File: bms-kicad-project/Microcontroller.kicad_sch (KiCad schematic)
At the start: 40 parts, among them J1 12402012E212A, J2 DEBUG, J3 Conn_02x18_Odd_Even, J4 Conn_02x18_Odd_Even, Q1 BSS308PE_H6327, SW1 KMR223G LFG, SW2 KMR223G LFG, U2 W25Q128JVSIQ TR, U3 NCP1117ST33T3G, U4 RP2040, X1 ABM8-272-T3

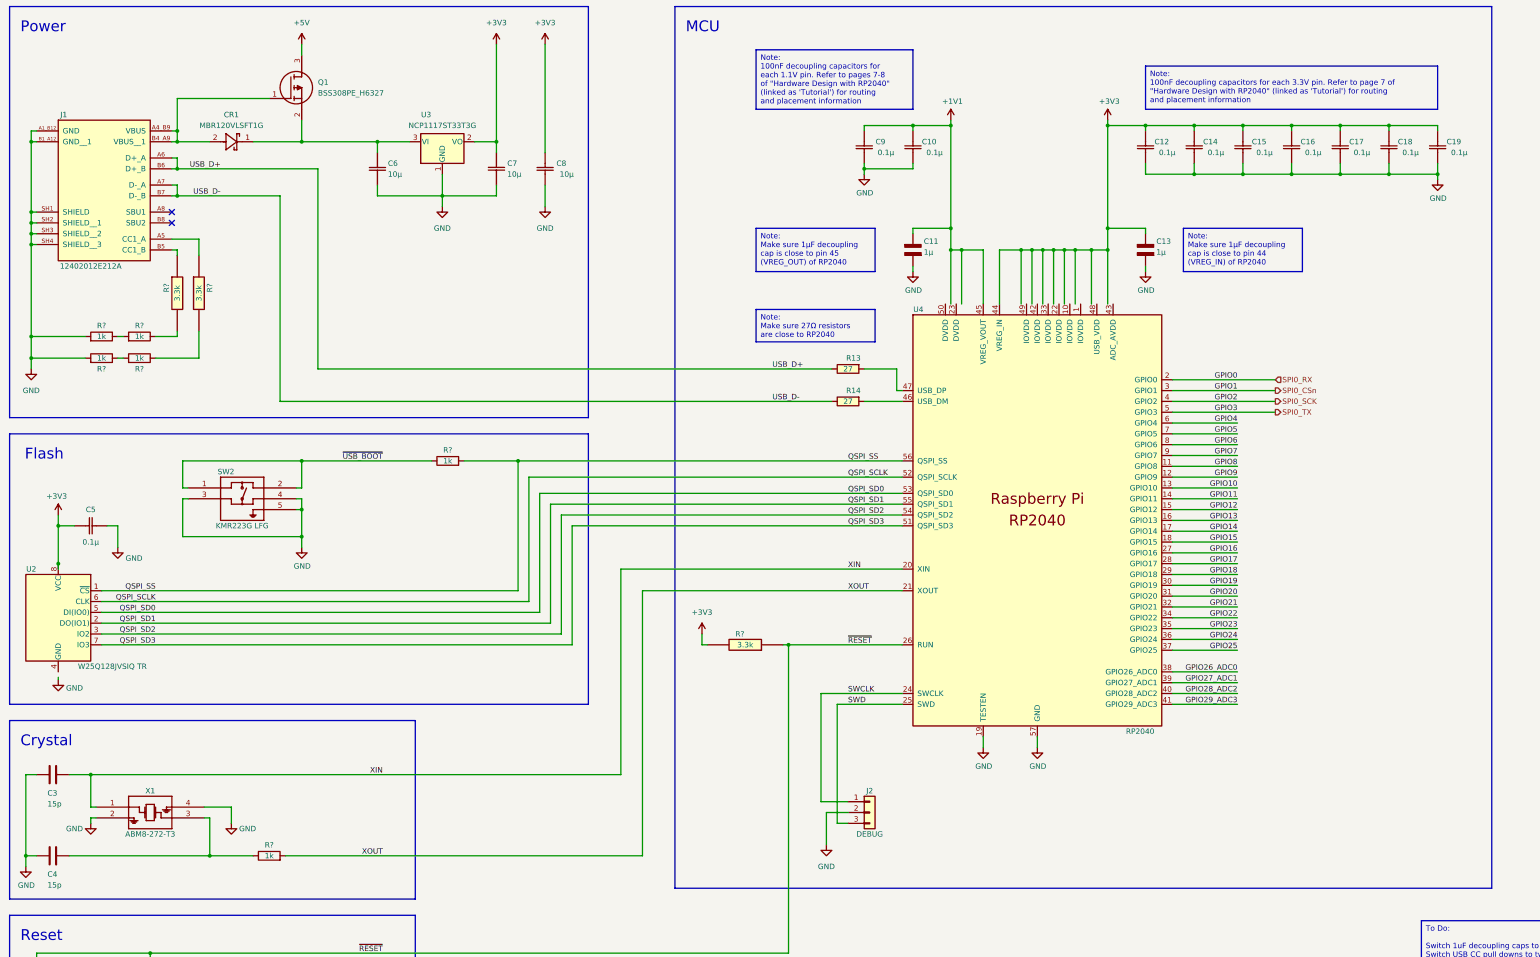
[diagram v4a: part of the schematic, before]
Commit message: feat: Added snubber circuit to 5V Regulator schematic
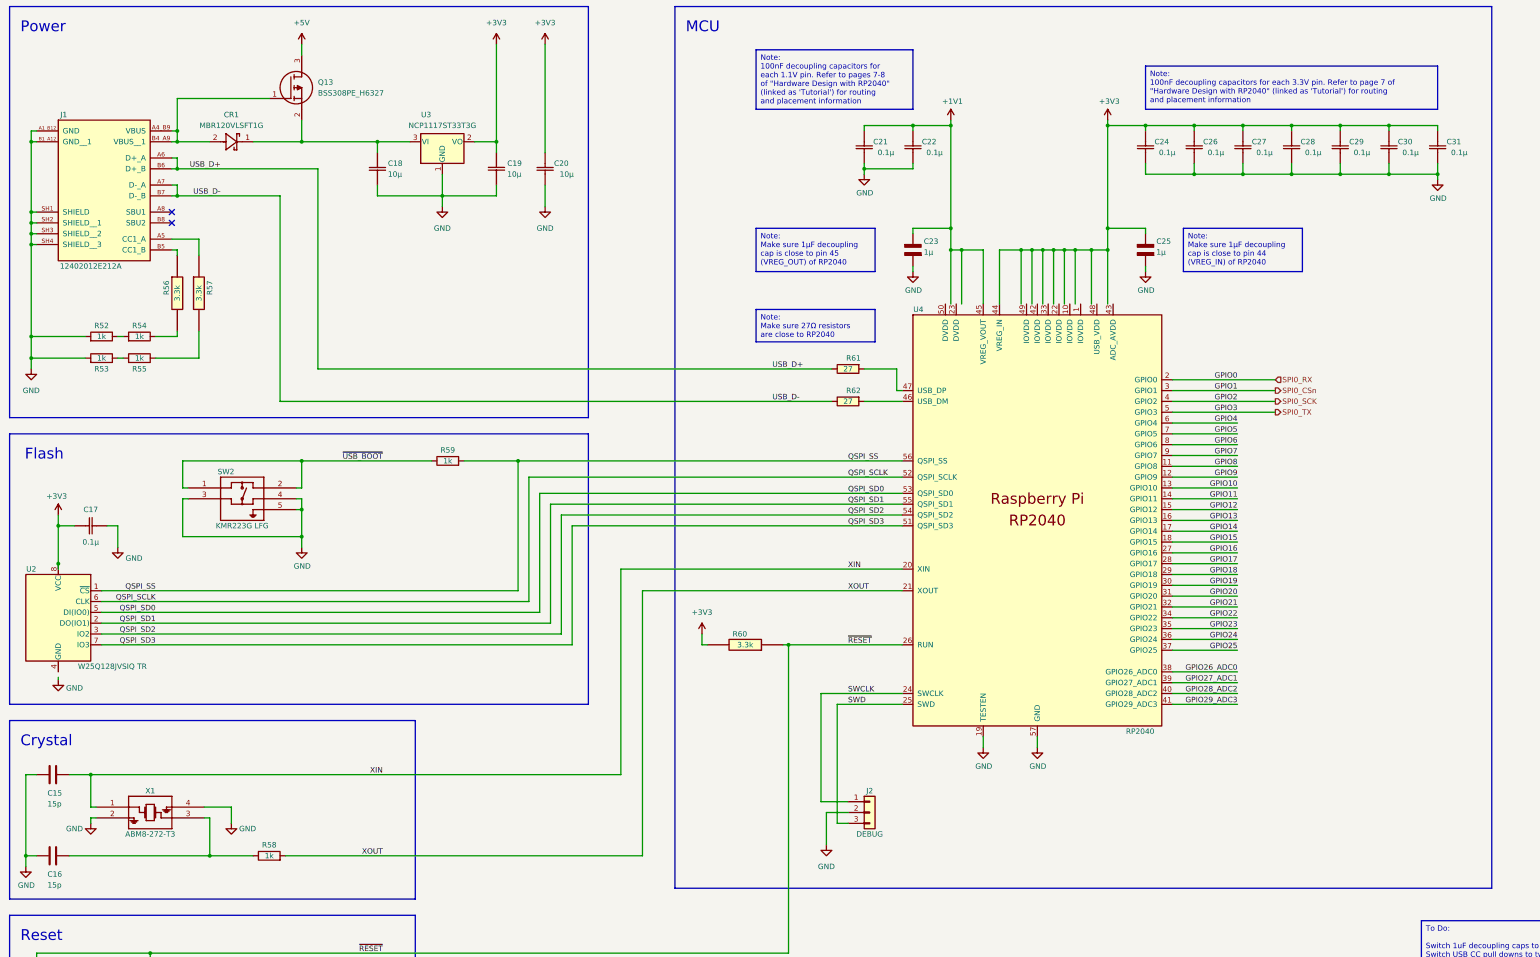
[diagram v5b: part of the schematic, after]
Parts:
- gave numbers to parts that had none: 9
- renumbered C3 to C15, C4 to C16, C5 to C17, C6 to C18, C7 to C19, C8 to C20, C9 to C21, C10 to C22, C11 to C23, C12 to C24, C13 to C25, C14 to C26, C15 to C27, C16 to C28, C17 to C29, C18 to C30, C19 to C31, Q1 to Q13, R13 to R61, R14 to R62

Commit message: feat: added buncha shit, refer to tasks 4 and 8
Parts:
- removed R52, R53, R54, R55: 1k, FixedWing:RC0805N_YAG, symbol FixedWing:RC0805FR-071KL
- removed R56, R57, R60: 3.3k, RESC2012X50N, symbol FixedWing:CRCW08053K30JNEA
- added R77, R78, R81: 5.6k, FixedWing:RESC2012X60N, symbol FixedWing:RK73H2ATTD5601F
- renumbered R58 to R79, R59 to R80, R61 to R82, R62 to R83
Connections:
- net +3V3: now also R81.1
- net GND: now also R77.1, R78.1
- net ~{RESET}: now also R81.2
- net at J1.A5 (CC1_A): now also R78.2
- net at J1.B5 (CC1_B): now also R77.2

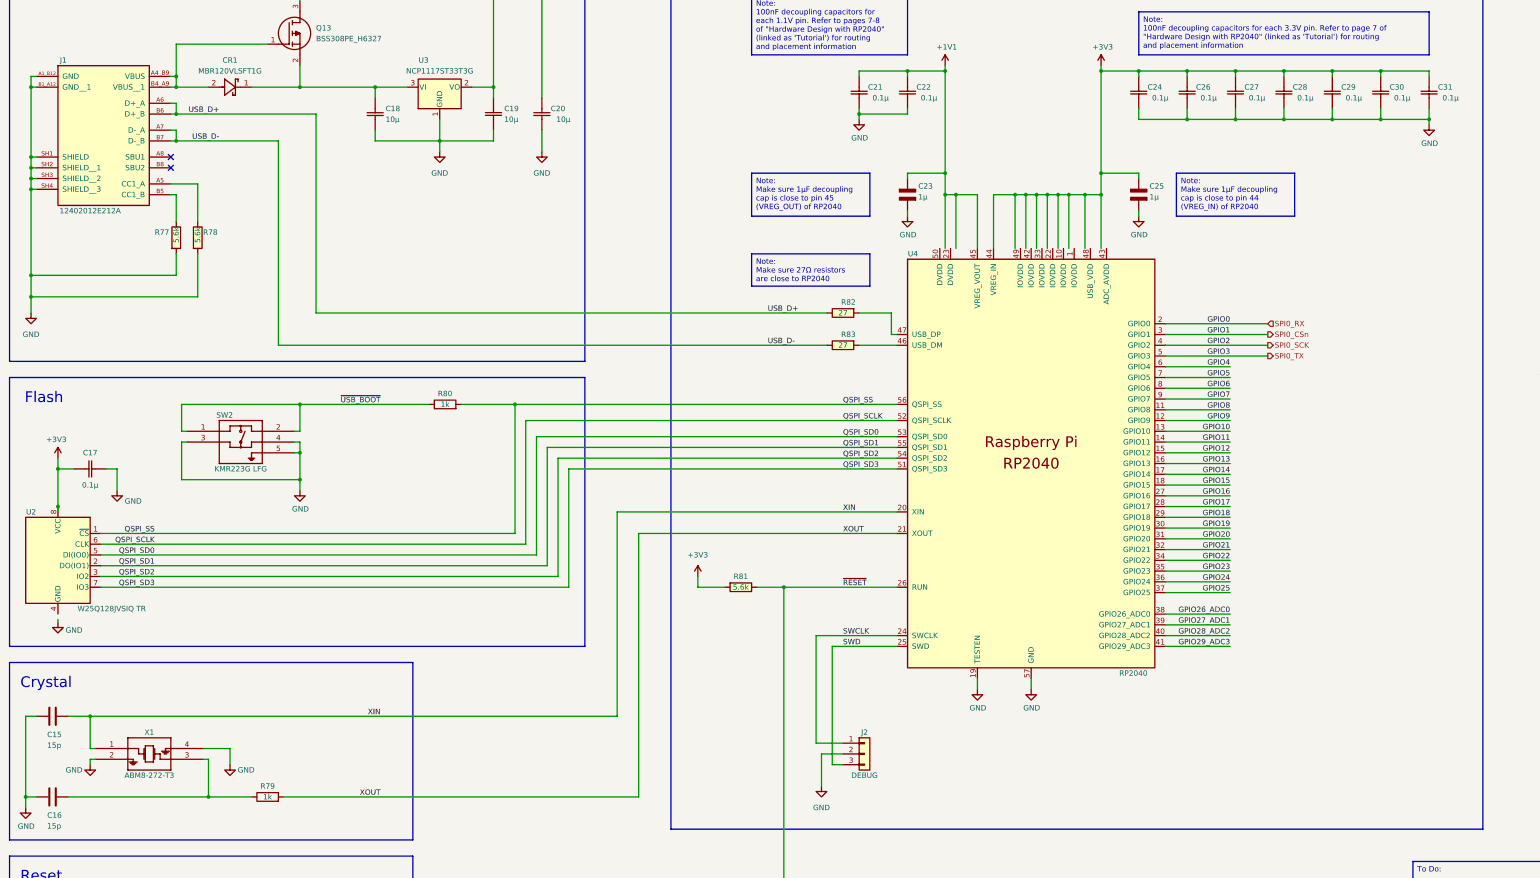
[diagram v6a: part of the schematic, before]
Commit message: feat: finished 5V reg circuit lgtm!
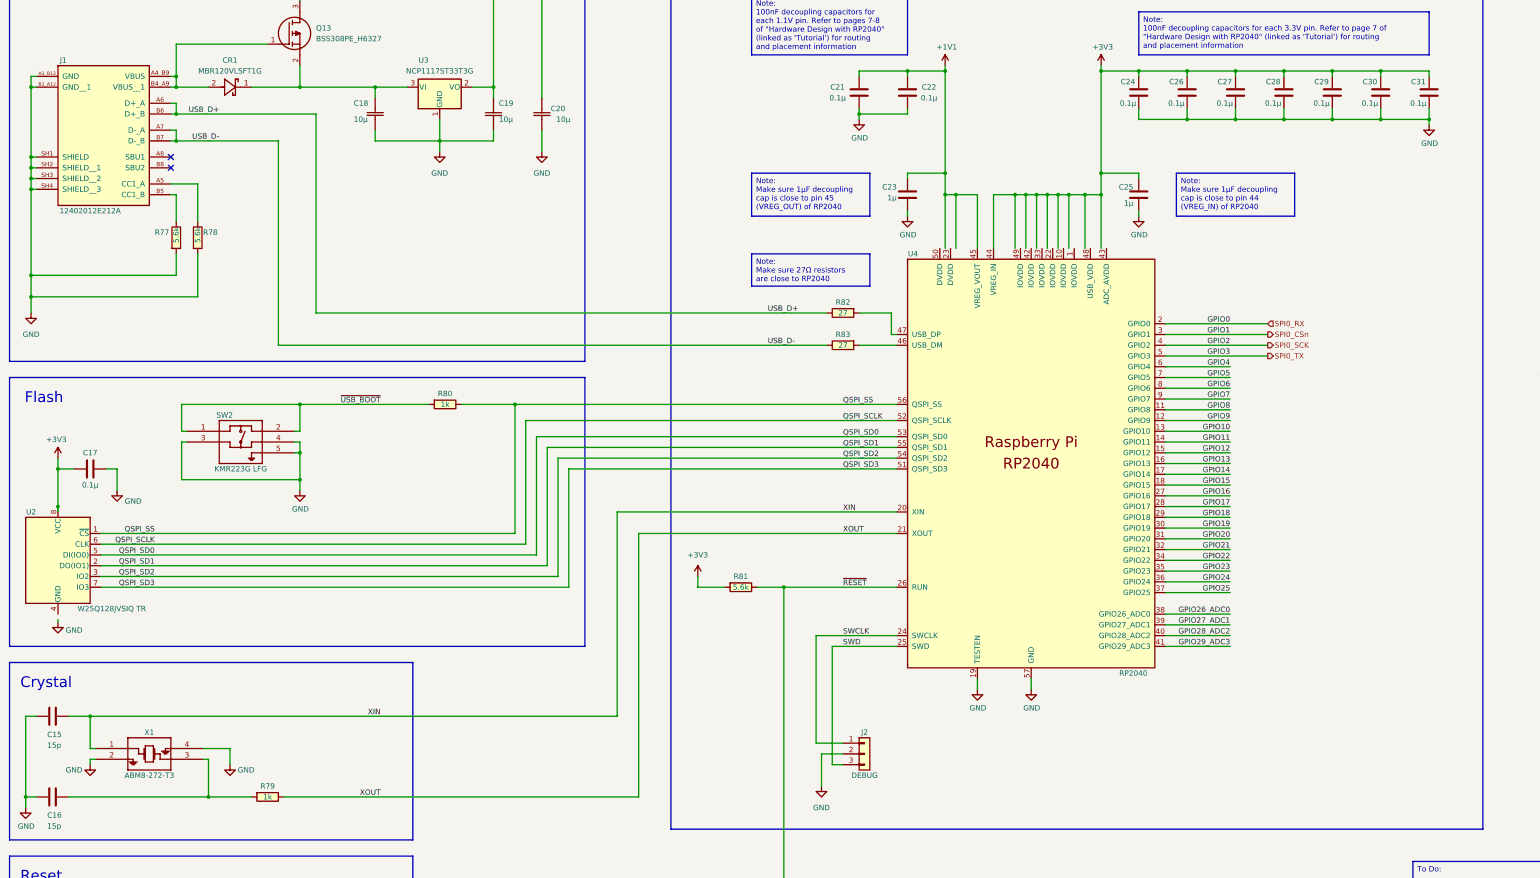
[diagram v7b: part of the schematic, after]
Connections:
- net +3V3: now also C17.1, C19.2, C24.1, C26.1, C28.1, C29.1, C30.1, C31.1; no longer C17.2, C19.1, C24.2, C26.2, C28.2, C29.2, C30.2, C31.2
- net GND: now also C17.2, C18.2, C19.1, C24.2, C26.2, C28.2, C29.2, C30.2, C31.2; no longer C17.1, C18.1, C19.2, C24.1, C26.1, C28.1, C29.1, C30.1, C31.1
- net at CR1.1, Q13.2 (S), U3.3 (VI): now also C18.1; no longer C18.2
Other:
- moved on the sheet: C18, C19

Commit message: Feature/current sensor (#17)
* feat: making sure my git still works

* feat: figured out battery stack monitor V+ biasing. Refer to task 5 on the punchlist for more details.

* feat: swapped out battery<->18V diode for cheaper alternative

* feat: started a new sheet for external connections and added current sensor

* feat: made a placeholder label to connect current sensor to LTC6811 GPIO

* feat: added remaining connectors to component library

* Wired up most external connections

* feat: Just shifting a few things around
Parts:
- removed CR1: MBR120VLSFT1G, FixedWing:DIOM3616X98N, symbol FixedWing:MBR120VLSFT1G
- added D4: B130LAW-7-F, FixedWing:SOD3716X145N, symbol FixedWing:B130LAW-7-F
- added LED13: LTST-C170KGKT, FixedWing:LED_LTST-C170KGKT_LTO, symbol FixedWing:LTST-C170KGKT
- added R91: 475, RESC2012X50N, symbol FixedWing:CRCW0805475RFKEA
- renumbered C15 to C22, C16 to C23, C17 to C24, C18 to C25, C19 to C26, C20 to C27, C21 to C28, C22 to C29, C23 to C30, C24 to C31, C25 to C32, C26 to C33, C27 to C34, C28 to C35, C29 to C36, C30 to C37, C31 to C38, J1 to J2, J2 to J3, J3 to J4, J4 to J5, Q13 to Q14, R77 to R84, R78 to R85, R79 to R86, R80 to R87, R81 to R88, R82 to R89, R83 to R90, U2 to U4, U3 to U5, U4 to U6
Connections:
- net +1V1: now also U6.23 (DVDD), U6.50 (DVDD)
- net +3V3: now also U6.1 (IOVDD), U6.10 (IOVDD), U6.22 (IOVDD), U6.33 (IOVDD), U6.42 (IOVDD), U6.43 (ADC_AVDD), U6.48 (USB_VDD), U6.49 (IOVDD)
- net GND: now also LED13.1 (K)
- net GPIO25: now also R91.1
- net at J2.A4_B9 (VBUS), J2.B4_A9 (VBUS__1), Q14.1 (G): now also D4.2 (A)
- net at C25.1, Q14.2 (S), U5.3 (VI): now also D4.1 (K)
- net GPIO4 renamed PIXDAT
- net GPIO5 renamed PIXCLK
- net GPIO6 renamed 4S_OR_LESS
- net GPIO7 renamed LEDOUT
- new net: LED13.2 (A), R91.2
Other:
- moved on the sheet: C28, C29
